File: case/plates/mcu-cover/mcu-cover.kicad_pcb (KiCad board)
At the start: 2 copper layers, 30.6 x 52.9 mm, 3 parts

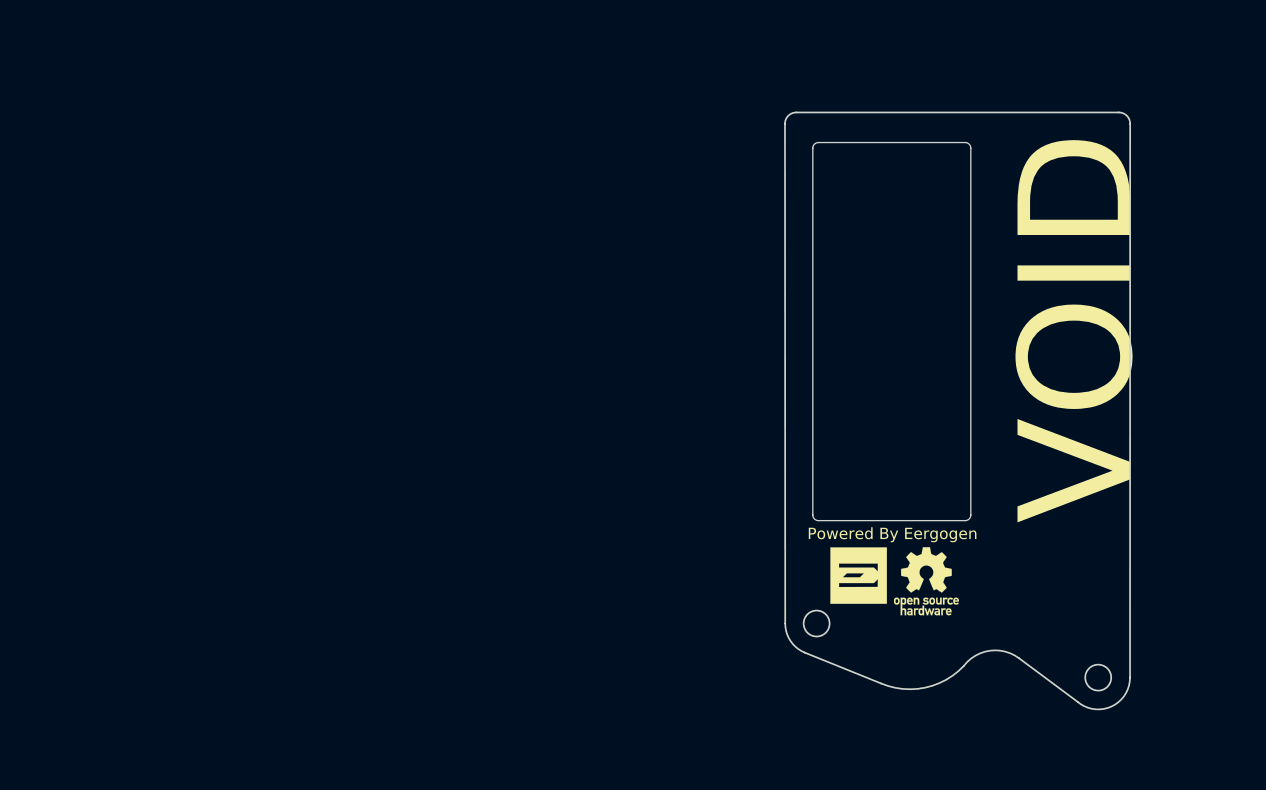
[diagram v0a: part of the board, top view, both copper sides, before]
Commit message: fixed mcu window size
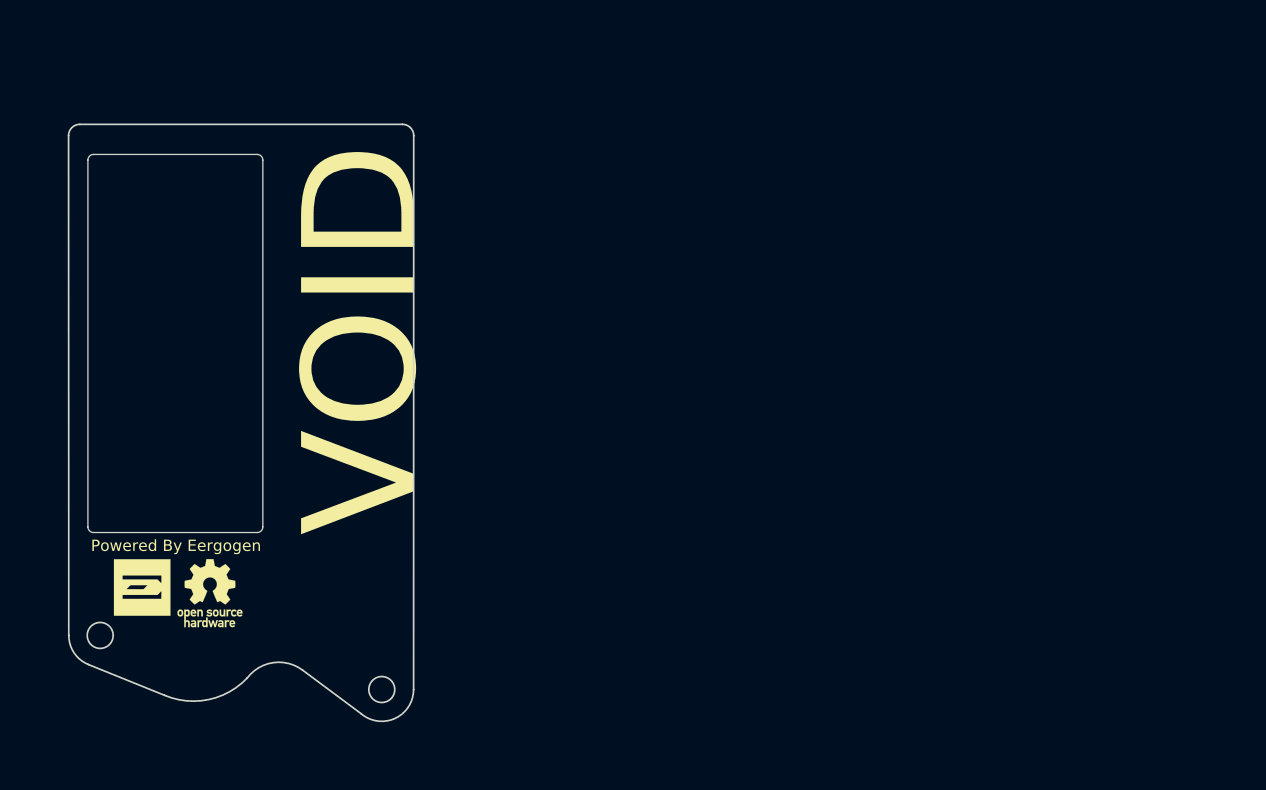
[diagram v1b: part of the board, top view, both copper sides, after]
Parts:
- moved DISP1 63.5 mm to (82.1, 69.0)
- moved LOGO1 63.5 mm to (79.1, 92.2)
- moved LOGO2 63.5 mm to (85.1, 92.7)
